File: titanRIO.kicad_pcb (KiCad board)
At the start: 4 copper layers, 55 parts, among them IC1 SLG46110V, J1 Screw_Terminal_01x02, J10 Conn_01x04, J11 Screw_Terminal_01x02, J12 Conn_01x10, J13 Conn_01x10, J14 Conn_01x10, J18 Screw_Terminal_01x02, J19 Conn_02x03_Odd_Even, J2 Conn_01x10, J20 Conn_01x10, J3 Conn_01x05, J5 Conn_01x02, J6 Conn_01x04, J7 LOOP0, J8 LOOP1, J9 Conn_01x05, Q2 BSS138, Q3 BSS138, Q4 BSS138, SW2 SW_DIP_x03, U1 Tang_Nano_20K, U2 TCAN332G, U3 MCP2518FD-xQBB, U4 PCA9685BS, U5 SN74LVC8T245PWR, U6 SN74LVC8T245PWR, Y1 Crystal

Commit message: Started on design, minor touch ups on schematic
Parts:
- removed IC1: SLG46110V, Samacsys:SLG46110V
- removed J19: Conn_02x03_Odd_Even, Connector_PinHeader_2.54mm:PinHeader_2x03_P2.54mm_Vertical
- removed J2: Conn_01x10, Connector_JST:JST_GH_BM10B-GHS-TBT_1x10-1MP_P1.25mm_Vertical
- removed R13, R7: 10K, Resistor_SMD:R_0805_2012Metric_Pad1.20x1.40mm_HandSolder
- added C1: 105uF, Capacitor_SMD:C_0201_0603Metric_Pad0.64x0.40mm_HandSolder, F.Cu at (39.5, 125.0)
- added C10: 470nF, Capacitor_SMD:C_0201_0603Metric_Pad0.64x0.40mm_HandSolder, F.Cu at (169.4, 145.0)
- added C11: 10nF C0G, Capacitor_SMD:C_0201_0603Metric_Pad0.64x0.40mm_HandSolder, F.Cu at (180.5, 141.5)
- added C12: 100nF, Capacitor_SMD:C_0201_0603Metric_Pad0.64x0.40mm_HandSolder, F.Cu at (179.9, 128.7)
- added C13: 100nF, Capacitor_SMD:C_0201_0603Metric_Pad0.64x0.40mm_HandSolder, F.Cu at (175.1, 149.5)
- added C14: 100nF, Capacitor_SMD:C_0201_0603Metric_Pad0.64x0.40mm_HandSolder, F.Cu at (177.9, 119.7)
- added C6: 470uF, Capacitor_SMD:CP_Elec_6.3x5.4_Nichicon, F.Cu at (39.3, 129.5)
- added C7: 180uF, Capacitor_SMD:CP_Elec_6.3x5.4_Nichicon, F.Cu at (72.0, 143.8)
- added C8: 180uF, Capacitor_SMD:CP_Elec_6.3x5.4_Nichicon, F.Cu at (72.0, 131.3)
- added D7: SS32, Diode_SMD:D_SMA, F.Cu at (55.0, 145.3)
- added D8: SS32, Diode_SMD:D_SMA, F.Cu at (55.0, 134.5)
- added D9: SS32, Diode_SMD:D_SMA, F.Cu at (157.5, 24.0)
- added J15: Screw_Terminal_01x02, TerminalBlock_Phoenix:TerminalBlock_Phoenix_MPT-0,5-2-2.54_1x02_P2.54mm_Horizontal, F.Cu at (51.5, 179.8)
- added J4: Conn_02x02_Odd_Even, Connector_PinHeader_2.54mm:PinHeader_2x02_P2.54mm_Vertical, F.Cu at (30.0, 51.3)
- added JP2: SolderJumper_2_Open, Jumper:SolderJumper-2_P1.3mm_Open_TrianglePad1.0x1.5mm, F.Cu at (173.2, 129.0)
- added L1: 68uH, Inductor_SMD:L_Bourns-SRU8028_8.0x8.0mm, F.Cu at (63.0, 143.5)
- added L2: 68uH, Inductor_SMD:L_Bourns-SRU8028_8.0x8.0mm, F.Cu at (63.0, 131.5)
- added R14: 0.1, Resistor_SMD:R_2816_7142Metric_Pad3.20x4.45mm_HandSolder, F.Cu at (36.1, 135.9)
- added R15: 10K, Resistor_SMD:R_0603_1608Metric_Pad0.98x0.95mm_HandSolder, F.Cu at (169.1, 143.5)
- added R16: 10K, Resistor_SMD:R_0603_1608Metric_Pad0.98x0.95mm_HandSolder, F.Cu at (165.5, 44.5)
- added R17: 470k, Resistor_SMD:R_0603_1608Metric_Pad0.98x0.95mm_HandSolder, F.Cu at (169.0, 147.5)
- added R18: 18k, Resistor_SMD:R_0603_1608Metric_Pad0.98x0.95mm_HandSolder, F.Cu at (181.0, 144.0)
- added R19: 10K, Resistor_SMD:R_0603_1608Metric_Pad0.98x0.95mm_HandSolder, F.Cu at (159.0, 125.6)
- added R20: 10K, Resistor_SMD:R_0603_1608Metric_Pad0.98x0.95mm_HandSolder, F.Cu at (178.4, 121.2)
- added R21: 10K, Resistor_SMD:R_0603_1608Metric_Pad0.98x0.95mm_HandSolder, F.Cu at (179.4, 127.2)
- added SW3: SW_Push, Button_Switch_SMD:SW_Push_1P1T_NO_CK_KMR2, F.Cu at (178.4, 124.2)
- added U11: 74LVC2G08, Package_SO:VSSOP-8_2.3x2mm_P0.5mm, F.Cu at (178.9, 117.7)
- added U12: XL1509-3.3, Package_SO:SOIC-8_3.9x4.9mm_P1.27mm, F.Cu at (48.1, 143.0)
- added U13: XL1509-5.0, Package_SO:SOIC-8_3.9x4.9mm_P1.27mm, F.Cu at (47.9, 131.2)
- added U14: INA219AxD, Package_SO:SOIC-8_3.9x4.9mm_P1.27mm, F.Cu at (37.1, 144.4)
- added U16: 74LVC1G175, Relay_THT:Relay_SPDT_Panasonic_DR-L2, F.Cu at (105.2, 126.1)
- added U17: 74HC123, Package_SO:SOP-16_4.4x10.4mm_P1.27mm, F.Cu at (175.1, 143.1)
- added Y2: SG-3031CM, Oscillator:Oscillator_SMD_SeikoEpson_SG3030CM, F.Cu at (147.0, 140.5)
- BNO08x1: footprint 0my_project:BNO086_PinSocket -> Connector_PinSocket_2.54mm:PinSocket_1x10_P2.54mm_Vertical
- C2, C3, C4, C5: footprint Capacitor_SMD:C_1206_3216Metric -> Capacitor_SMD:C_0201_0603Metric_Pad0.64x0.40mm_HandSolder
- J5: value Conn_01x02 -> Screw_Terminal_01x02; footprint Connector_JST:JST_GH_BM02B-GHS-TBT_1x02-1MP_P1.25mm_Vertical -> TerminalBlock_Phoenix:TerminalBlock_Phoenix_MPT-0,5-2-2.54_1x02_P2.54mm_Horizontal
- J7: value LOOP0 -> Screw_Terminal_01x02; footprint Connector_JST:JST_GH_BM02B-GHS-TBT_1x02-1MP_P1.25mm_Vertical -> TerminalBlock_Phoenix:TerminalBlock_Phoenix_MPT-0,5-2-2.54_1x02_P2.54mm_Horizontal
- J8: value LOOP1 -> Conn_01x12; footprint Connector_JST:JST_GH_BM02B-GHS-TBT_1x02-1MP_P1.25mm_Vertical -> Connector_JST:JST_GH_BM12B-GHS-TBT_1x12-1MP_P1.25mm_Vertical
- R10, R11, R12, R4, R8, R9: footprint Resistor_SMD:R_0805_2012Metric_Pad1.20x1.40mm_HandSolder -> Resistor_SMD:R_0603_1608Metric_Pad0.98x0.95mm_HandSolder
- R5, R6: footprint Resistor_SMD:R_0805_2012Metric_Pad1.20x1.40mm_HandSolder -> Resistor_SMD:R_1812_4532Metric_Pad1.30x3.40mm_HandSolder
- moved J20 192.6 mm to (22.6, 80.9), turned to 90 degrees
- moved J1 151.0 mm to (24.5, 138.4), turned to 90 degrees
- moved J11 140.8 mm to (24.5, 131.4), turned to 90 degrees
- moved C5 118.7 mm to (42.5, 167.7), turned to 180 degrees
- moved U3 112.8 mm to (43.6, 164.7), turned to 180 degrees
- moved D3 110.0 mm to (50.0, 171.8), turned to -90 degrees
- moved J3 107.6 mm to (198.9, 43.0), turned to -90 degrees
- moved JP1 106.6 mm to (50.3, 185.8), turned to 0 degrees
- moved U2 105.4 mm to (50.0, 166.6)
- moved R5 104.9 mm to (44.0, 180.3)
- moved C3 102.1 mm to (55.0, 169.0), turned to 0 degrees
- moved R6 100.9 mm to (56.0, 180.3), turned to -90 degrees
- moved C4 100.4 mm to (50.0, 163.8), turned to 180 degrees
- moved Y1 94.0 mm to (55.5, 165.1), turned to -90 degrees
- moved C2 89.0 mm to (55.0, 161.1), turned to 0 degrees
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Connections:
- A1 pad 36: +3V3 -> unconnected-(A1-3V3-Pad36)
- A1 pad 39: VCC -> +5V
- D1 pad 1: VCC -> +5V
- D3 pad 1: Net-(J5-Pin_1) -> Net-(J15-Pin_1)
- D3 pad 2: Net-(J5-Pin_2) -> Net-(J15-Pin_2)
- J1 pad 1: VCC -> GND
- J1 pad 2: GND -> Net-(J1-Pin_2)
- J11 pad 1: VCC -> GND
- J11 pad 2: GND -> Net-(J11-Pin_2)
- J13 pad 10: Net-(J13-Pin_10) -> GND
- J14 pad 2: VCC -> +5V
- J7 pad 1: LOOP0IN -> Net-(J5-Pin_2)
- J7 pad 2: LOOP0OUT -> Net-(J7-Pin_2)
- J8 pad 1: LOOP1IN -> GND
- J8 pad 2: LOOP1OUT -> SCL
- Q3 pad 1: Net-(J2-Pin_9) -> Net-(J8-Pin_9)
- R1 pad 1: VCC -> +5V
- R11 pad 2: Net-(J2-Pin_9) -> Net-(J8-Pin_9)
- R12 pad 1: GND -> ~{ACTIVE}
- R12 pad 2: ACTIVE -> +3V3
- R4 pad 2: VCC -> +5V
- R5 pad 1: Net-(J5-Pin_2) -> Net-(J15-Pin_2)
- R6 pad 1: Net-(J5-Pin_1) -> Net-(J15-Pin_1)
- SW2 pad 1: LOOP0IN -> +3V3
- SW2 pad 2: WDI_OVR -> Net-(J5-Pin_1)
- SW2 pad 3: LOOP1OUT -> Net-(J5-Pin_2)
- SW2 pad 4: LOOP1IN -> Net-(J7-Pin_2)
- SW2 pad 5: GND -> Net-(J5-Pin_2)
- SW2 pad 6: LOOP0OUT -> Net-(R15-Pad2)
- U1 pad 19: +3V3 -> unconnected-(U1-3V3-Pad19)
- U1 pad 25: +3V3 -> unconnected-(U1-3V3-Pad25)
- U1 pad 40: VCC -> Net-(D9-K)
- U2 pad 6: Net-(J5-Pin_2) -> Net-(J15-Pin_2)
- U2 pad 7: Net-(J5-Pin_1) -> Net-(J15-Pin_1)
- U4 pad 25: VCC -> +3V3
- U4 pad 26: GND -> +3V3
- U4 pad 27: GND -> +3V3
- U4 pad 28: GND -> +3V3
- U5 pad 11: Net-(J13-Pin_10) -> GND
- U5 pad 12: Net-(J13-Pin_10) -> GND
- U5 pad 13: Net-(J13-Pin_10) -> GND
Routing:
- net GND: track 0.00 -> 171.2 mm
- net +3V3: track 0.00 -> 152.8 mm
- net Net-(J11-Pin_2): track 0.00 -> 65.4 mm
- net Net-(J12-Pin_1): track 0.00 -> 37.0 mm
- net +5V: track 0.00 -> 25.9 mm
- net Net-(A1-GPIO26_ADC0): track 0.00 -> 21.4 mm
- net Net-(J15-Pin_2): track 0.00 -> 19.6 mm
- net Net-(J15-Pin_1): track 0.00 -> 18.4 mm
- net Net-(J1-Pin_2): track 0.00 -> 16.7 mm
- net Net-(U3-OSC2): track 0.00 -> 15.9 mm
- net Net-(A1-GPIO27_ADC1): track 0.00 -> 15.8 mm
- net CAN_INT: track 0.00 -> 14.3 mm
- net Net-(D7-K): track 0.00 -> 14.3 mm
- net Net-(U3-OSC1): track 0.00 -> 13.9 mm
- net Net-(J13-Pin_1): track 0.00 -> 13.5 mm
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
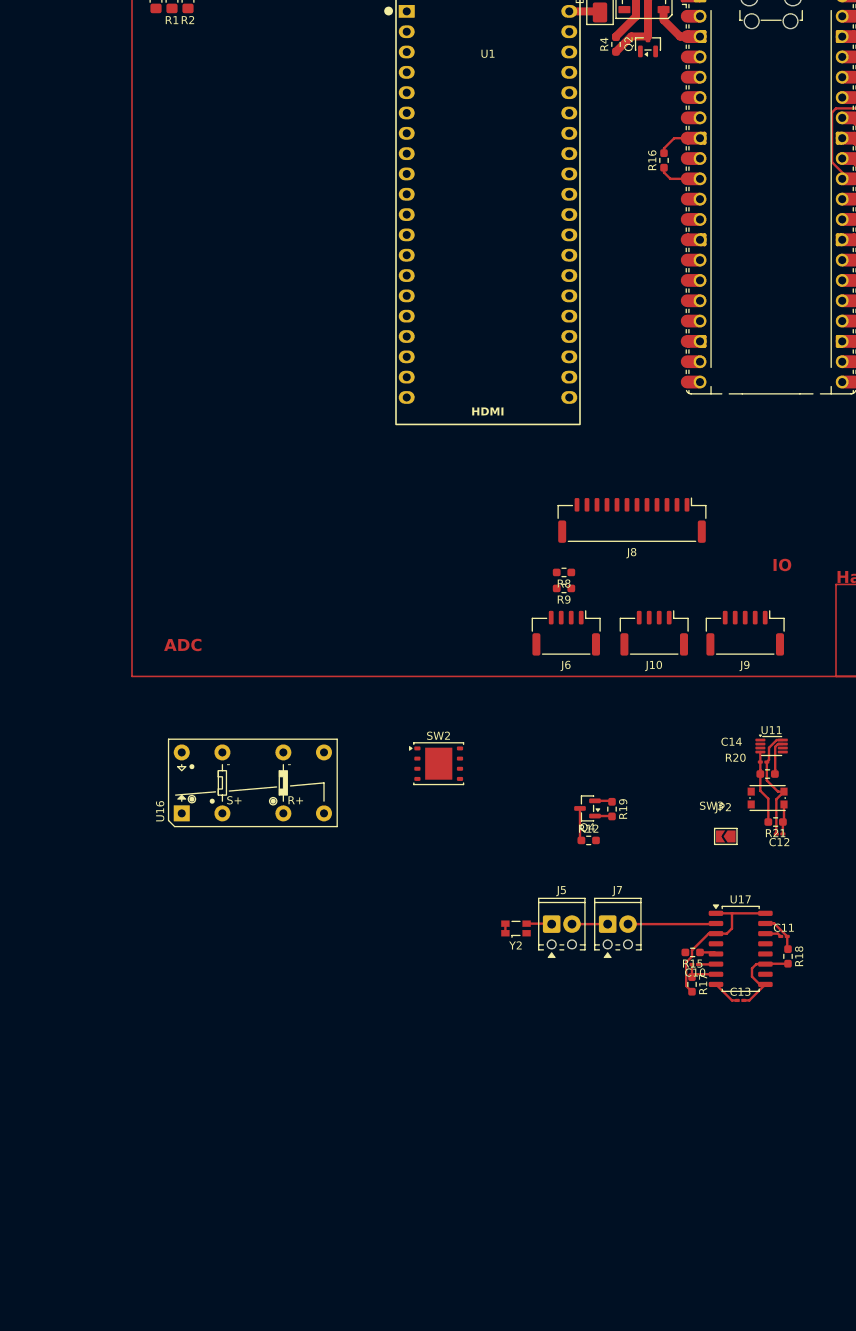
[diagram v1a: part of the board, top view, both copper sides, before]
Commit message: Did prospective safety circuit design. Terminals are backwards, remember to fix.
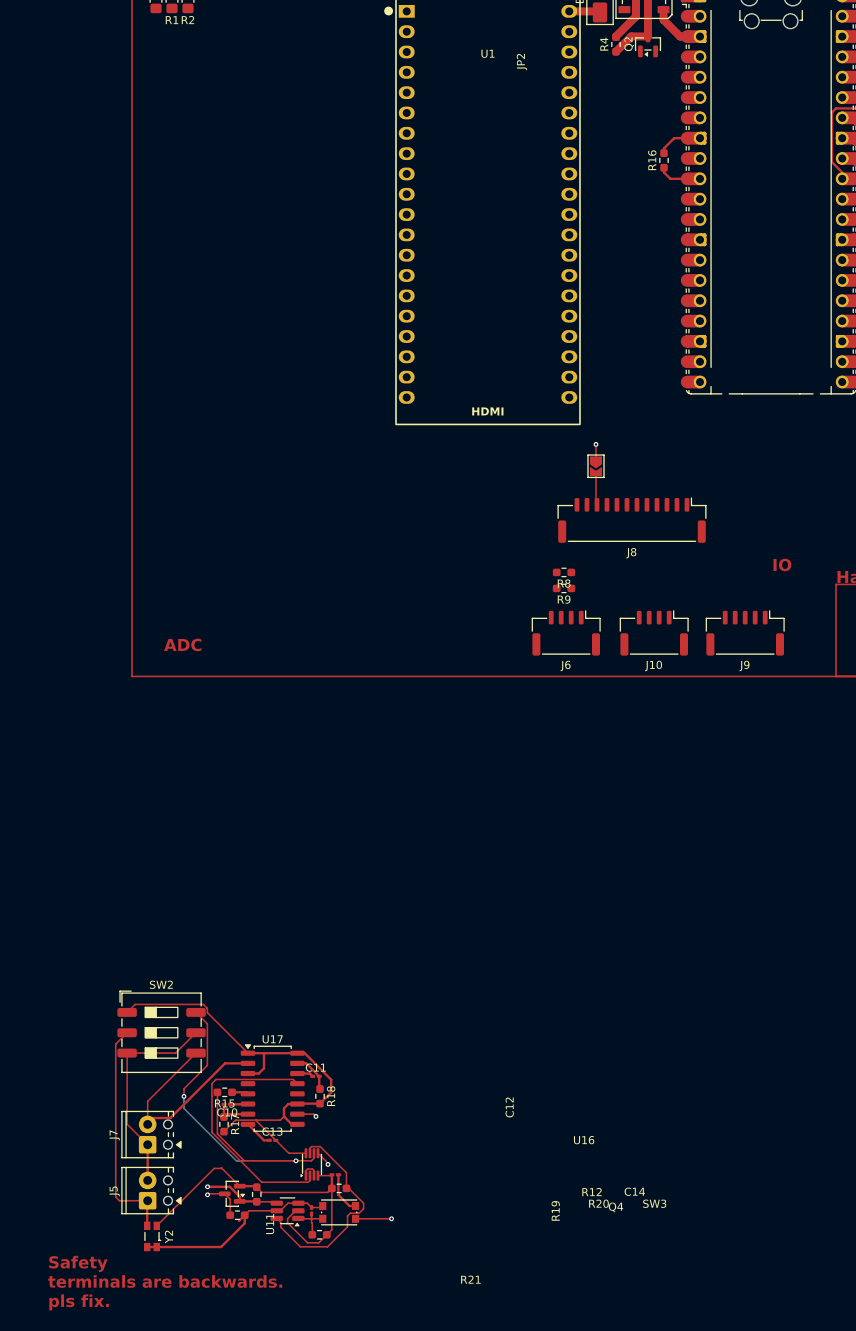
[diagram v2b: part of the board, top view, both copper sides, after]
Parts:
- SW2: footprint Package_SON:WSON-8-1EP_6x5mm_P1.27mm_EP3.4x4mm -> Button_Switch_SMD:SW_DIP_SPSTx03_Slide_9.78x9.8mm_W8.61mm_P2.54mm
- U16: footprint Relay_THT:Relay_SPDT_Panasonic_DR-L2 -> Package_TO_SOT_SMD:SOT-23-6_Handsoldering
- moved U11 77.7 mm to (121.5, 170.0), turned to 90 degrees
- moved R21 76.9 mm to (122.4, 178.8), turned to 0 degrees
- moved C12 75.1 mm to (121.4, 175.8), turned to 90 degrees
- moved R20 74.5 mm to (124.9, 173.0)
- moved SW3 74.5 mm to (124.9, 176.0)
- moved C14 74.4 mm to (124.4, 171.3)
- moved Q4 65.5 mm to (111.5, 173.7)
- moved R19 65.5 mm to (114.6, 173.8)
- moved R12 64.2 mm to (112.2, 176.3)
- moved J7 63.8 mm to (101.0, 167.5), turned to 90 degrees
- moved J5 61.2 mm to (101.0, 174.5), turned to 90 degrees
- moved C10 61.1 mm to (110.9, 162.5)
- moved C11 61.1 mm to (122.0, 159.0)
- moved C13 61.1 mm to (116.6, 167.0)
- moved R15 61.1 mm to (110.6, 161.0)
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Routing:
- net Net-(R15-Pad2): track 0.00 -> 50.3 mm, vias 0 -> 2
- net +3V3: track 152.8 -> 199.4 mm
- net GND: track 171.2 -> 204.7 mm
- net Net-(U17A-Q): track 0.00 -> 33.4 mm
- net Net-(J5-Pin_1): track 3.16 -> 28.5 mm
- net Net-(U16-~{CLR}): track 4.01 -> 27.3 mm
- net Net-(J5-Pin_2): track 4.46 -> 26.9 mm
- net Net-(J7-Pin_2): track 11.0 -> 27.4 mm
- net CLR_FAULT: track 3.79 -> 12.3 mm, vias 0 -> 2
- net ACTIVE: track 2.15 -> 9.85 mm, vias 0 -> 1
- net Net-(J8-Pin_10): track 0.00 -> 4.15 mm
- net WDI_MASTER: track 0.00 -> 2.44 mm, vias 0 -> 1
- net Net-(U11-Pad1): track 0.00 -> 2.42 mm
- net RPI_READY: track 4.62 -> 6.54 mm, vias 0 -> 1
- net ~{ACTIVE}: track 4.07 -> 5.16 mm, vias 0 -> 1
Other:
- board text added: "Safety terminals are backwards. pls fix."

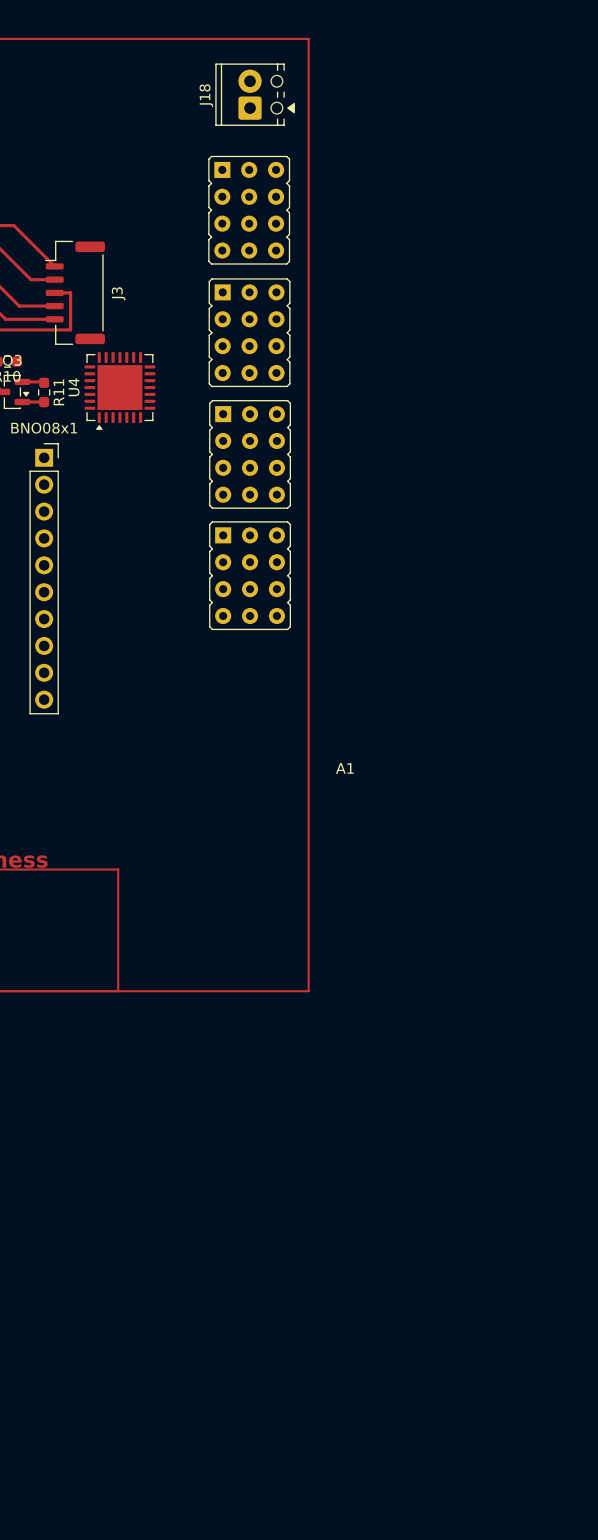
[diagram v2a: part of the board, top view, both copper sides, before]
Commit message: Wired up servo
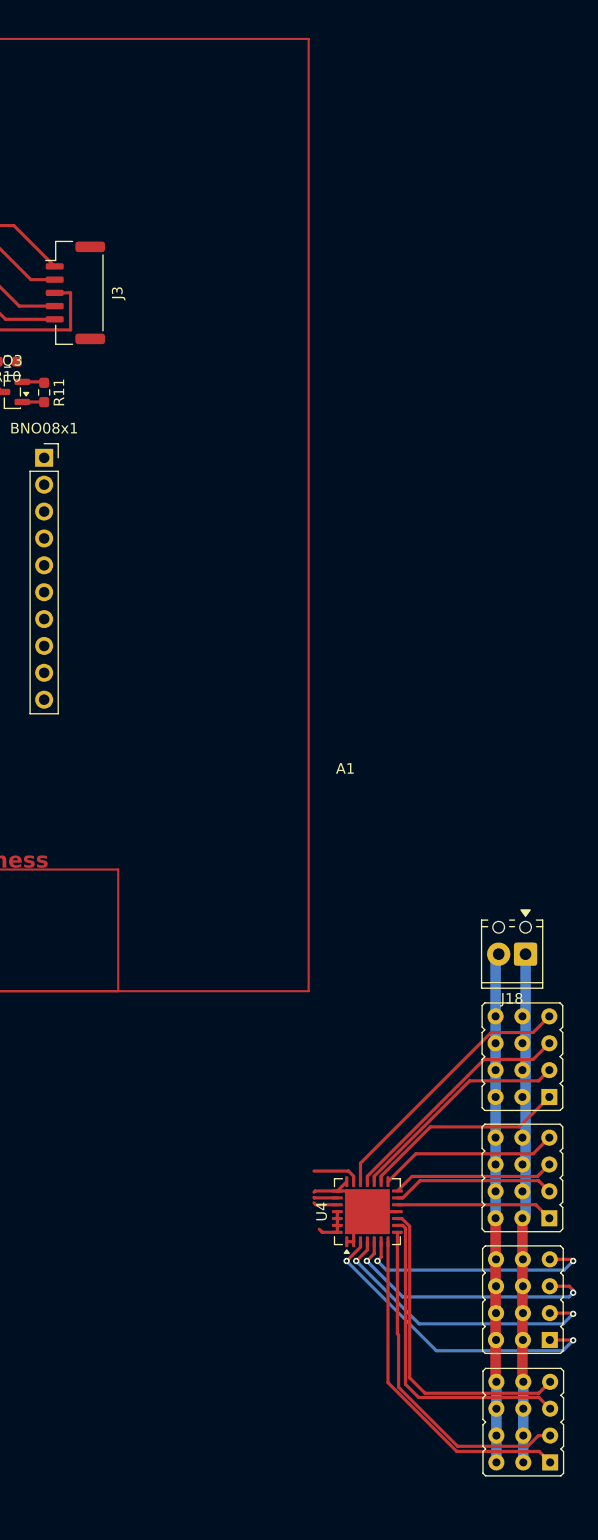
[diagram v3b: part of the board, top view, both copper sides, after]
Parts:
- moved U8 117.4 mm to (241.3, 149.7), turned to 180 degrees
- moved U7 95.0 mm to (241.2, 138.2), turned to 180 degrees
- moved J18 84.1 mm to (241.5, 105.5), turned to 180 degrees
- moved U4 81.3 mm to (226.6, 129.8)
- moved U9 73.1 mm to (241.2, 126.7), turned to 180 degrees
- moved U10 52.2 mm to (241.2, 115.2), turned to 180 degrees
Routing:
- net GND: track 204.7 -> 266.9 mm
- net Net-(J18-Pin_1): track 0.00 -> 48.2 mm
- net Net-(U4-LED4): track 0.00 -> 31.8 mm
- net Net-(U4-LED5): track 0.00 -> 31.7 mm
- net Net-(U4-LED6): track 0.00 -> 30.3 mm
- net Net-(U4-LED7): track 0.00 -> 30.1 mm
- net Net-(U4-LED0): track 0.00 -> 29.9 mm, vias 0 -> 2
- net Net-(U4-LED1): track 0.00 -> 27.8 mm, vias 0 -> 2
- net Net-(U4-LED2): track 0.00 -> 25.8 mm, vias 0 -> 2
- net Net-(U4-LED15): track 0.00 -> 25.3 mm
- net Net-(U4-LED3): track 0.00 -> 23.5 mm, vias 0 -> 2
- net Net-(U4-LED14): track 0.00 -> 22.9 mm
- net Net-(U4-LED13): track 0.00 -> 21.2 mm
- net Net-(U4-LED12): track 0.00 -> 19.5 mm
- net Net-(U4-LED11): track 0.00 -> 17.0 mm
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
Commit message: Fixed up minor mistakes and reversed terminals in psu. DO THE COPPER POUR, DAMNIT
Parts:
- moved SW3 29.4 mm to (110.5, 150.4), turned to 90 degrees
- moved C11 29.1 mm to (93.5, 153.2), turned to 90 degrees
- moved R20 28.6 mm to (107.5, 150.4), turned to 90 degrees
- moved R18 27.9 mm to (96.0, 152.8), turned to 0 degrees
- moved C14 27.7 mm to (105.8, 150.9), turned to 90 degrees
- moved R21 27.6 mm to (113.3, 152.8), turned to 90 degrees
- moved C12 24.7 mm to (110.3, 153.8), turned to 180 degrees
- moved SW2 24.0 mm to (88.0, 172.6), turned to 90 degrees
- moved U11 23.5 mm to (104.5, 153.8), turned to 180 degrees
- moved U17 21.7 mm to (95.0, 158.7), turned to 90 degrees
- moved U16 20.7 mm to (110.3, 156.8), turned to -90 degrees
- moved C13 17.2 mm to (101.5, 158.7), turned to 90 degrees
- moved R15 15.6 mm to (95.5, 164.7), turned to -90 degrees
- moved R19 14.6 mm to (108.2, 160.7), turned to 0 degrees
- moved C10 14.1 mm to (97.0, 164.3), turned to -90 degrees
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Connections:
- C1 pad 1: Net-(J11-Pin_2) -> Net-(U12-VIN)
- C6 pad 1: Net-(J11-Pin_2) -> Net-(U12-VIN)
- J11 pad 2: Net-(J11-Pin_2) -> Net-(J1-Pin_2)
- R14 pad 2: Net-(J11-Pin_2) -> Net-(U12-VIN)
- U12 pad 1: Net-(J11-Pin_2) -> Net-(U12-VIN)
- U13 pad 1: Net-(J11-Pin_2) -> Net-(U12-VIN)
- U14 pad 7: Net-(J11-Pin_2) -> Net-(U12-VIN)
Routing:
- net GND: track 266.9 -> 356.8 mm
- net Net-(J11-Pin_2): track 65.4 -> 0.00 mm
- net Net-(U12-VIN): track 0.00 -> 50.2 mm
- net +3V3: track 203.2 -> 230.1 mm
- net Net-(A1-GPIO26_ADC0): track 21.4 -> 2.25 mm
- net Net-(J1-Pin_2): track 16.7 -> 28.9 mm
- net Net-(A1-ADC_VREF): track 10.0 -> 0.00 mm
- net +5V: track 25.9 -> 35.3 mm
- net Net-(A1-GPIO28_ADC2): track 10.5 -> 3.35 mm
- net Net-(A1-AGND): track 9.99 -> 4.64 mm
- net RPI_READY: track 6.54 -> 2.51 mm
- net Net-(J5-Pin_1): track 28.5 -> 24.7 mm
- net Net-(A1-GPIO27_ADC1): track 15.8 -> 12.7 mm
- net Net-(A1-RUN): track 6.13 -> 3.29 mm
- net SDA_OUT: track 2.23 -> 4.46 mm, vias 0 -> 2
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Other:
- board text added: "Safety"
- board text removed: "Safety terminals are backwards. pls fix."

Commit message: Implementing just so much stuff. RP2350B on board, new sensors, PSU magic, buncha stuff
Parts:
- added JP3: Jumper_2_Bridged, acheron_Connectors:PinHeader_1x2_P2.54mm_Vertical, F.Cu at (104.9, 136.6)
- added U15: RP2350B-QFN80, Package_DFN_QFN:QFN-80-1EP_10x10mm_P0.4mm_EP3.4x3.4mm, F.Cu at (172.6, 144.4)
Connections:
- U17 pad 10: WDI_MASTER -> Net-(JP3-A)
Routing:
- net WDI_MASTER: track 2.44 -> 0.00 mm, vias 1 -> 0
- net Net-(JP3-A): track 0.00 -> 2.44 mm, vias 0 -> 1
